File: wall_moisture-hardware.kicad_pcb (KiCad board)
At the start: 4 copper layers, 78.5 x 99.3 mm, 46 parts, among them SW2 FSMH

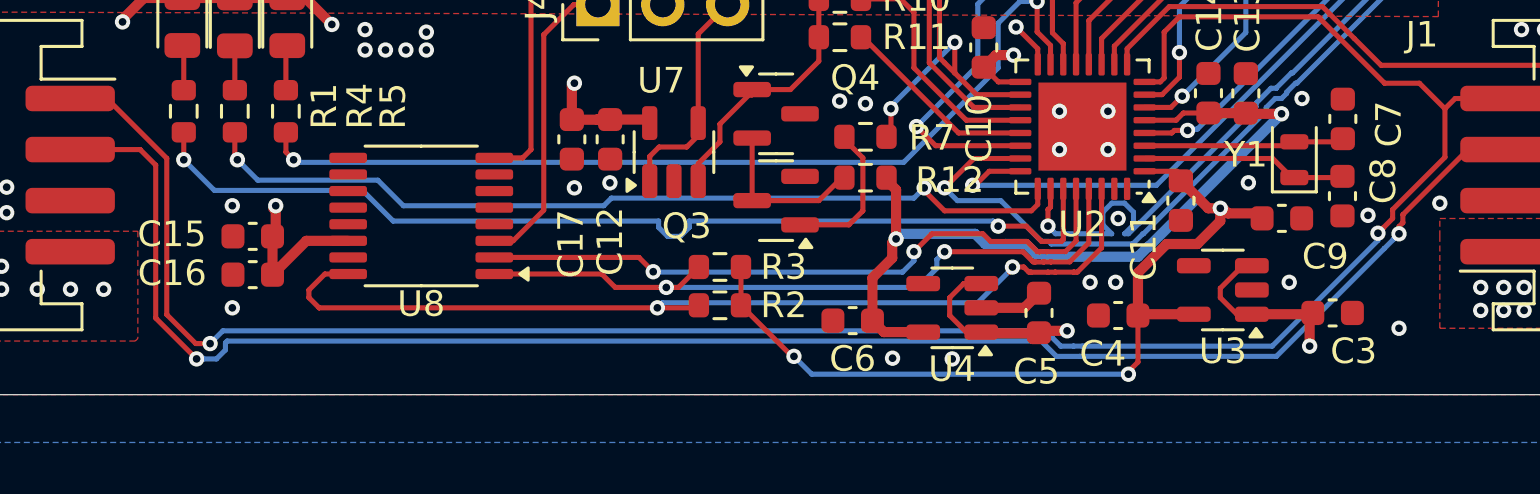
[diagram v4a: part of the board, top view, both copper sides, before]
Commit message: design: Move vias to enhance the 5V copper fill continuity and reduce the impedance
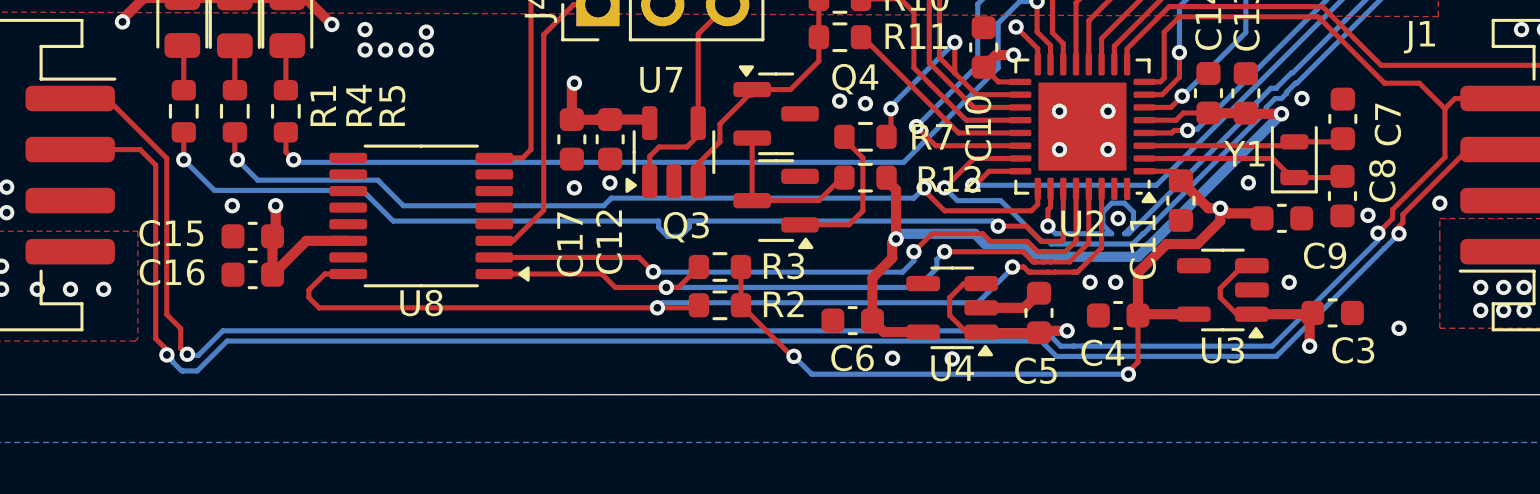
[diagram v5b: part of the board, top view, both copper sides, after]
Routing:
- net /Connectors and Power/MASTER_RX: track 85.2 -> 86.1 mm
- net /Connectors and Power/MASTER_TX: track 92.4 -> 93.1 mm
- net GND: vias 47 -> 46

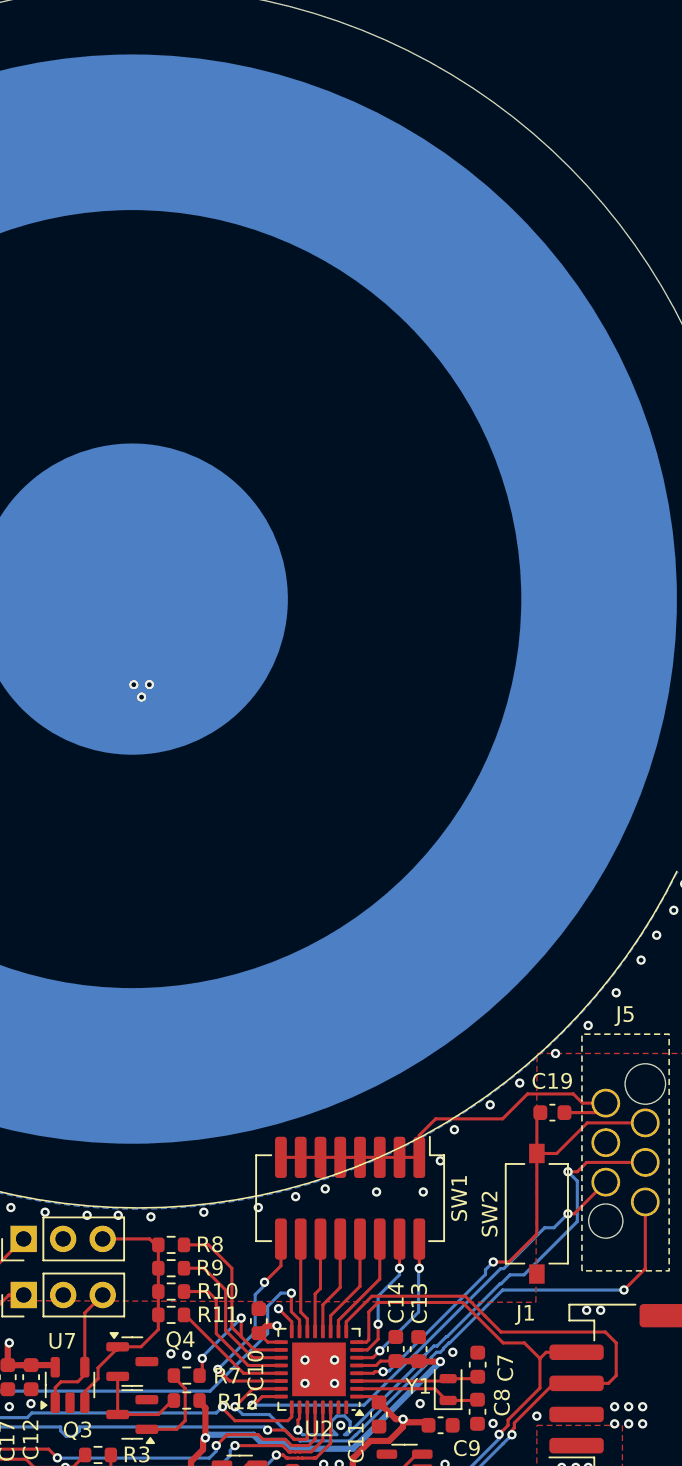
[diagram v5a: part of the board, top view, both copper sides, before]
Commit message: design: Propagate the changes to the PCB and change the tactile switch footprint
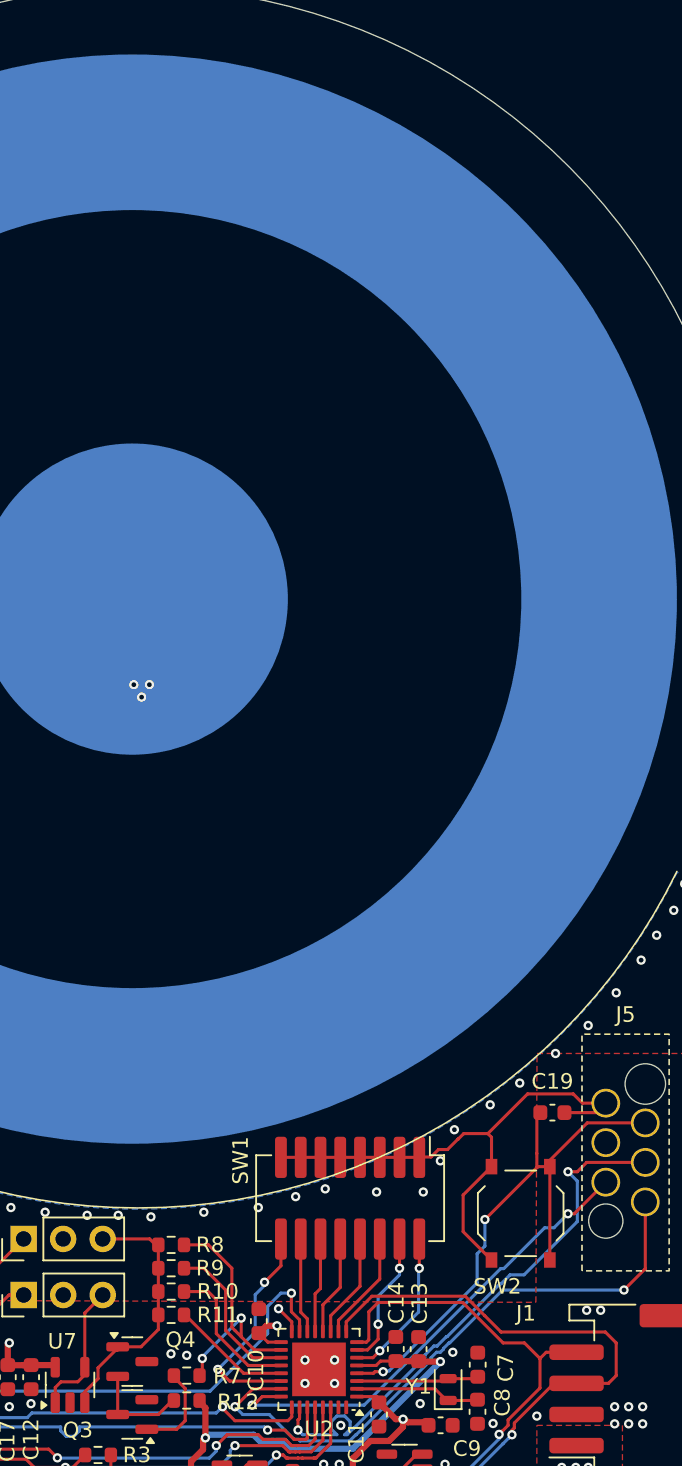
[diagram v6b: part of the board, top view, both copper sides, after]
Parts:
- R12: value 1k -> 2.2k
- R5: value 15 -> 100
- SW2: footprint footprints:SW_Tactile_SPST_NO_Straight_CK_PTS636Sx25SMTRLFS -> footprints:SW_Push_1P1T_XKB_TS-1187A
- moved SW2 1.04 mm to (121.3, 119.0)
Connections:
- net /µC and digital/LED_B renamed /µC and digital/LED_Y
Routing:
- net GND: track 55.8 -> 64.7 mm
- net /µC and digital/NRST: track 31.6 -> 37.2 mm
